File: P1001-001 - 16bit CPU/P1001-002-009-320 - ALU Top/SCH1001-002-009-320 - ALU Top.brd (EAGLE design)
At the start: 200 x 152 mm, 59 parts, among them IC27 MEGA8535-A, IC42 74ALS04D, IC55 74ALS04D

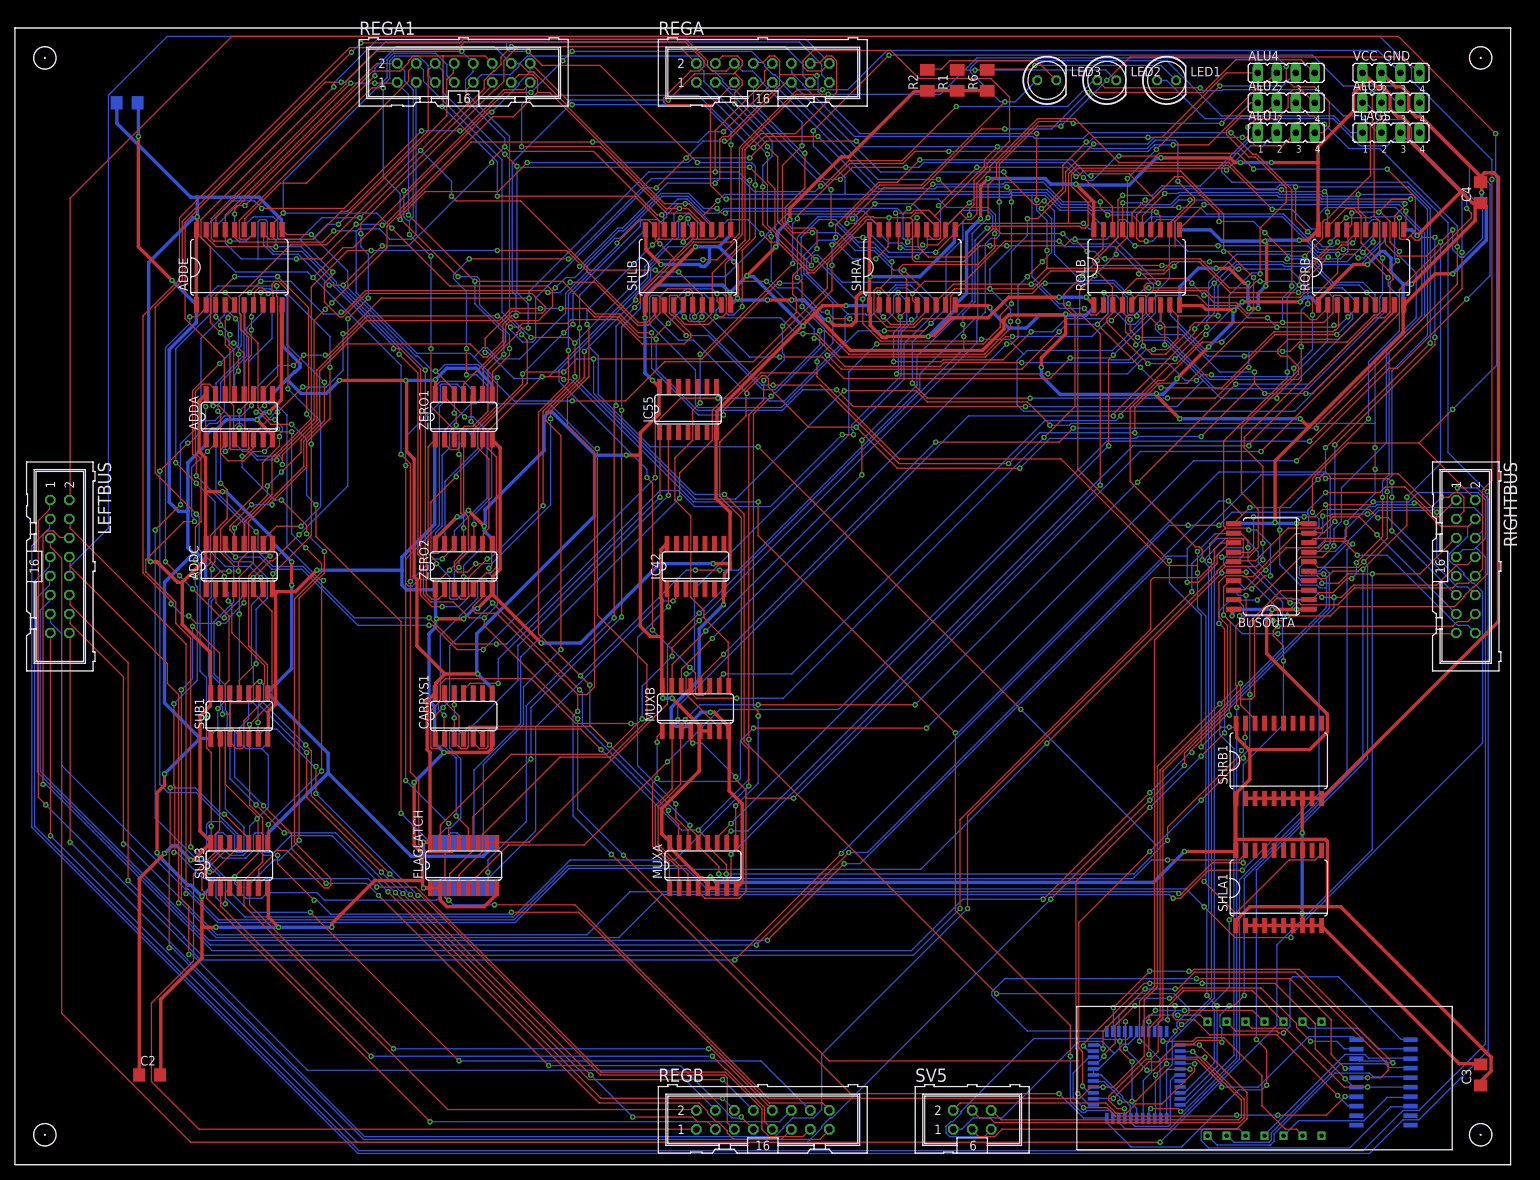
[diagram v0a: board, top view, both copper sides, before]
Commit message: add ram to Memory
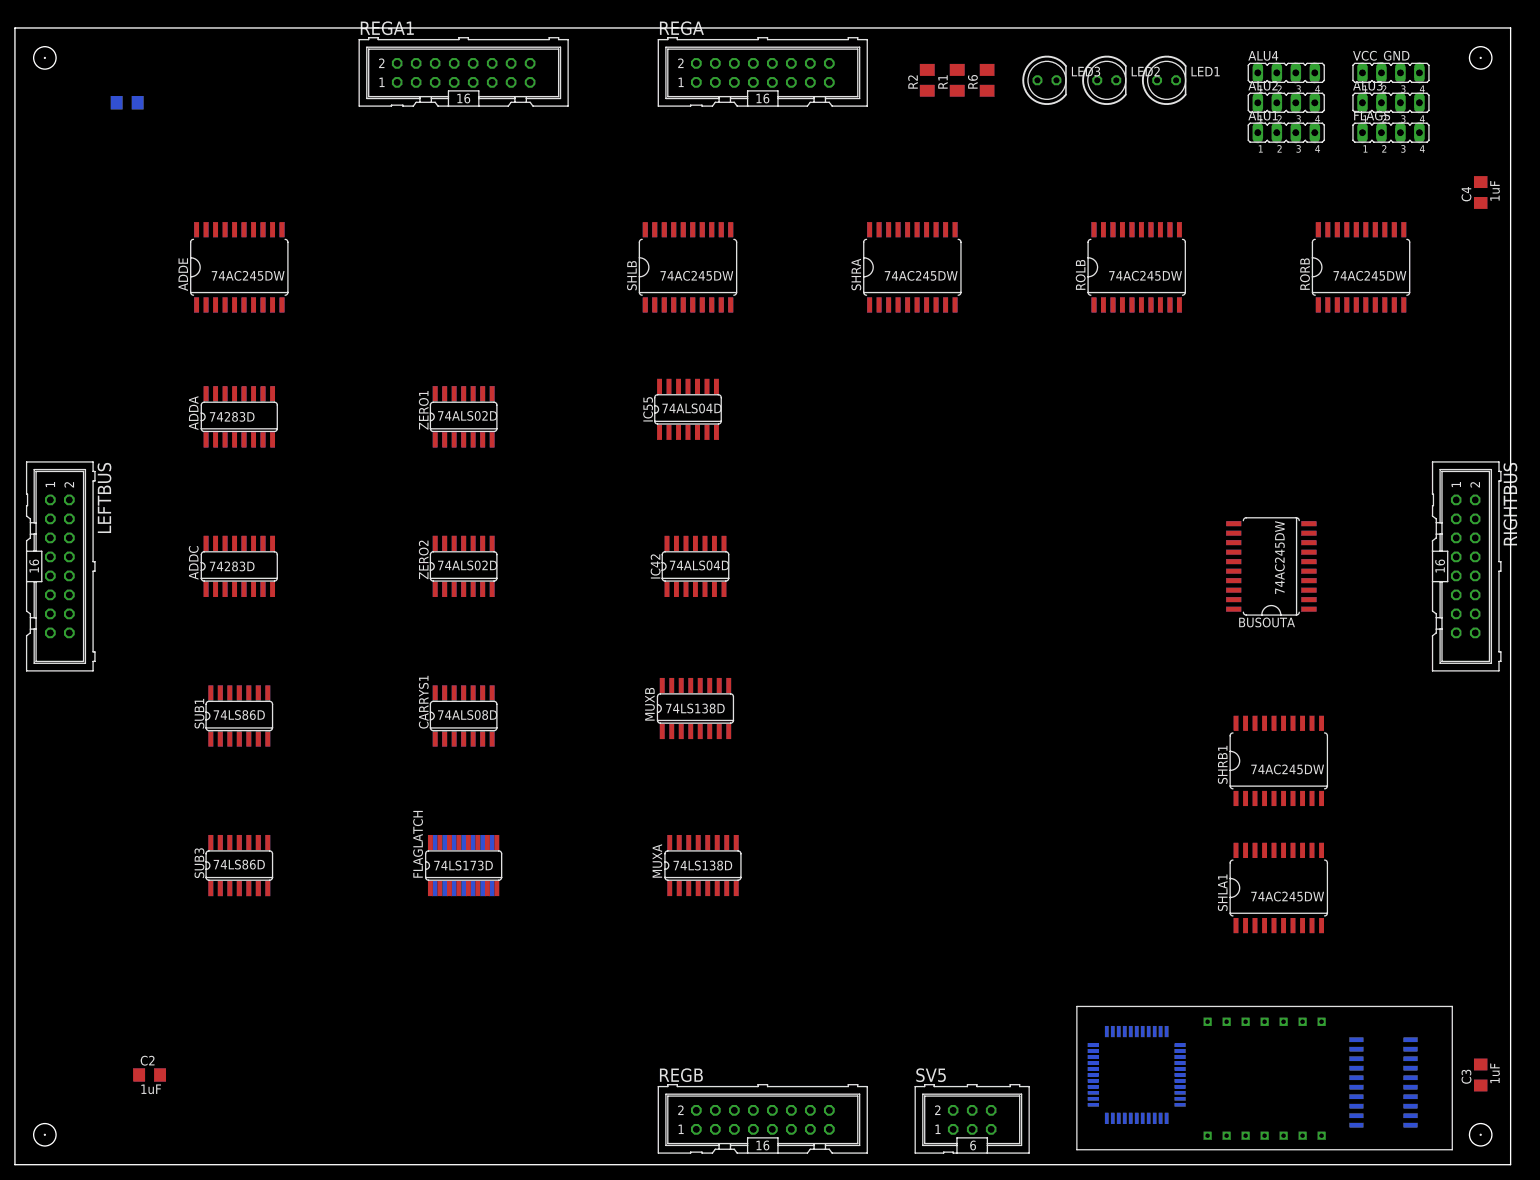
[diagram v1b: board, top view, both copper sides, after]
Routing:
- net VCC: track 1156.9 -> 0.00 mm, vias 52 -> 0
- net GND: track 1009.6 -> 0.00 mm, vias 44 -> 0
- net BUSOUT11: track 506.8 -> 0.00 mm, vias 15 -> 0
- net BUSOUT13: track 504.1 -> 0.00 mm, vias 18 -> 0
- net BUSOUT9: track 501.9 -> 0.00 mm, vias 19 -> 0
- net BUSOUT10: track 495.5 -> 0.00 mm, vias 16 -> 0
- net BUSOUT15: track 492.6 -> 0.00 mm, vias 17 -> 0
- net BUSOUT14: track 490.0 -> 0.00 mm, vias 20 -> 0
- net BUSOUT12: track 476.7 -> 0.00 mm, vias 21 -> 0
- net BUSOUT3: track 471.6 -> 0.00 mm, vias 11 -> 0
- net BUSOUT8: track 456.7 -> 0.00 mm, vias 21 -> 0
- net BUSOUT0: track 450.2 -> 0.00 mm, vias 20 -> 0
- net BUSOUT6: track 427.8 -> 0.00 mm, vias 18 -> 0
- net BUSOUT1: track 417.8 -> 0.00 mm, vias 18 -> 0
- net BUSOUT4: track 415.8 -> 0.00 mm, vias 19 -> 0
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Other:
- board text added: "BRD1001-002-009-320 A ALU Top"
- board text added: "Copyright 2020 James Wright"
